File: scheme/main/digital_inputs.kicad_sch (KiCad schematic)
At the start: 0 parts

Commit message: di & do terminals
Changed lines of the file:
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@@
 		)
 	)
-	(hierarchical_label "COM-"
-		(shape output)
+	(hierarchical_label "COM"
+		(shape input)
 		(at 163.83 93.98 0)
 		(fields_autoplaced yes)
@@
 	)
 	(hierarchical_label "DI2-"
-		(shape input)
+		(shape output)
 		(at 163.83 72.39 0)
 		(fields_autoplaced yes)
@@
 		)
 	)
-	(hierarchical_label "COM+"
+	(hierarchical_label "24V"
 		(shape output)
 		(at 163.83 57.15 0)
@@
 	)
 	(hierarchical_label "DI4-"
-		(shape input)
+		(shape output)
 		(at 163.83 88.9 0)
 		(fields_autoplaced yes)
@@
 	)
 	(hierarchical_label "DI1-"
-		(shape input)
+		(shape output)
 		(at 163.83 64.77 0)
 		(fields_autoplaced yes)
@@
 	)
 	(hierarchical_label "DI3-"
-		(shape input)
+		(shape output)
 		(at 163.83 81.28 0)
 		(fields_autoplaced yes)
@@
 			)
 		)
-		(pin "in-" input
+		(pin "in-" output
 			(at 125.73 85.09 0)
 			(effects
@@
 			)
 		)
-		(pin "in-" input
+		(pin "in-" output
 			(at 125.73 68.58 0)
 			(effects
@@
 			)
 		)
-		(pin "in-" input
+		(pin "in-" output
 			(at 125.73 53.34 0)
 			(effects
@@
 			)
 		)
-		(pin "in-" input
+		(pin "in-" output
 			(at 125.73 101.6 0)
 			(effects

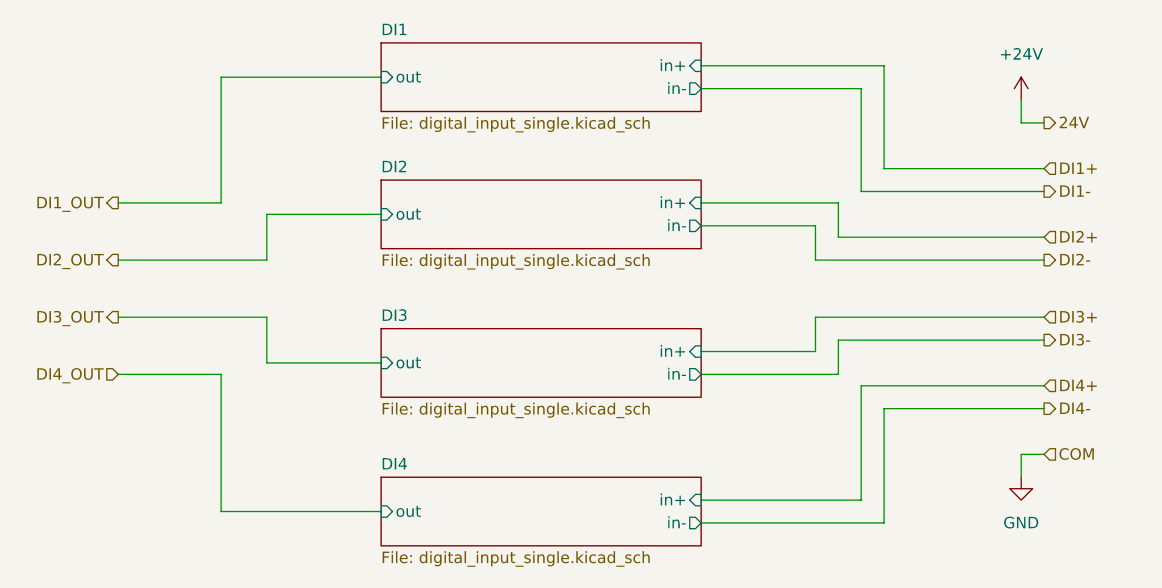
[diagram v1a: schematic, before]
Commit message: toplevel layout, can bus
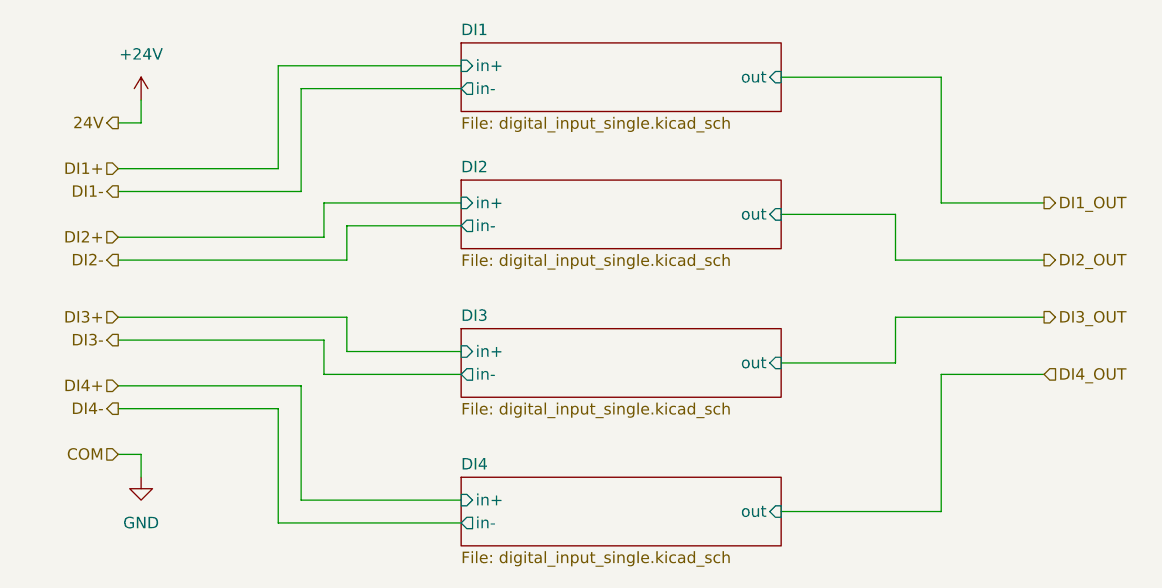
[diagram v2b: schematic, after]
